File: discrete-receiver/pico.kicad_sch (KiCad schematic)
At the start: 48 parts, among them SW1 Reset, SW2 Select, SW3 Enter, U12 TPS7A20xxxDBV, U13 LM66100DCK, U14 LM66100DCK, U15 LM66100DCK, U6 RP2350A, U7 W25Q128JVS, U8 NCP1117-3.3_SOT223, Y1 ABM8-272-T3

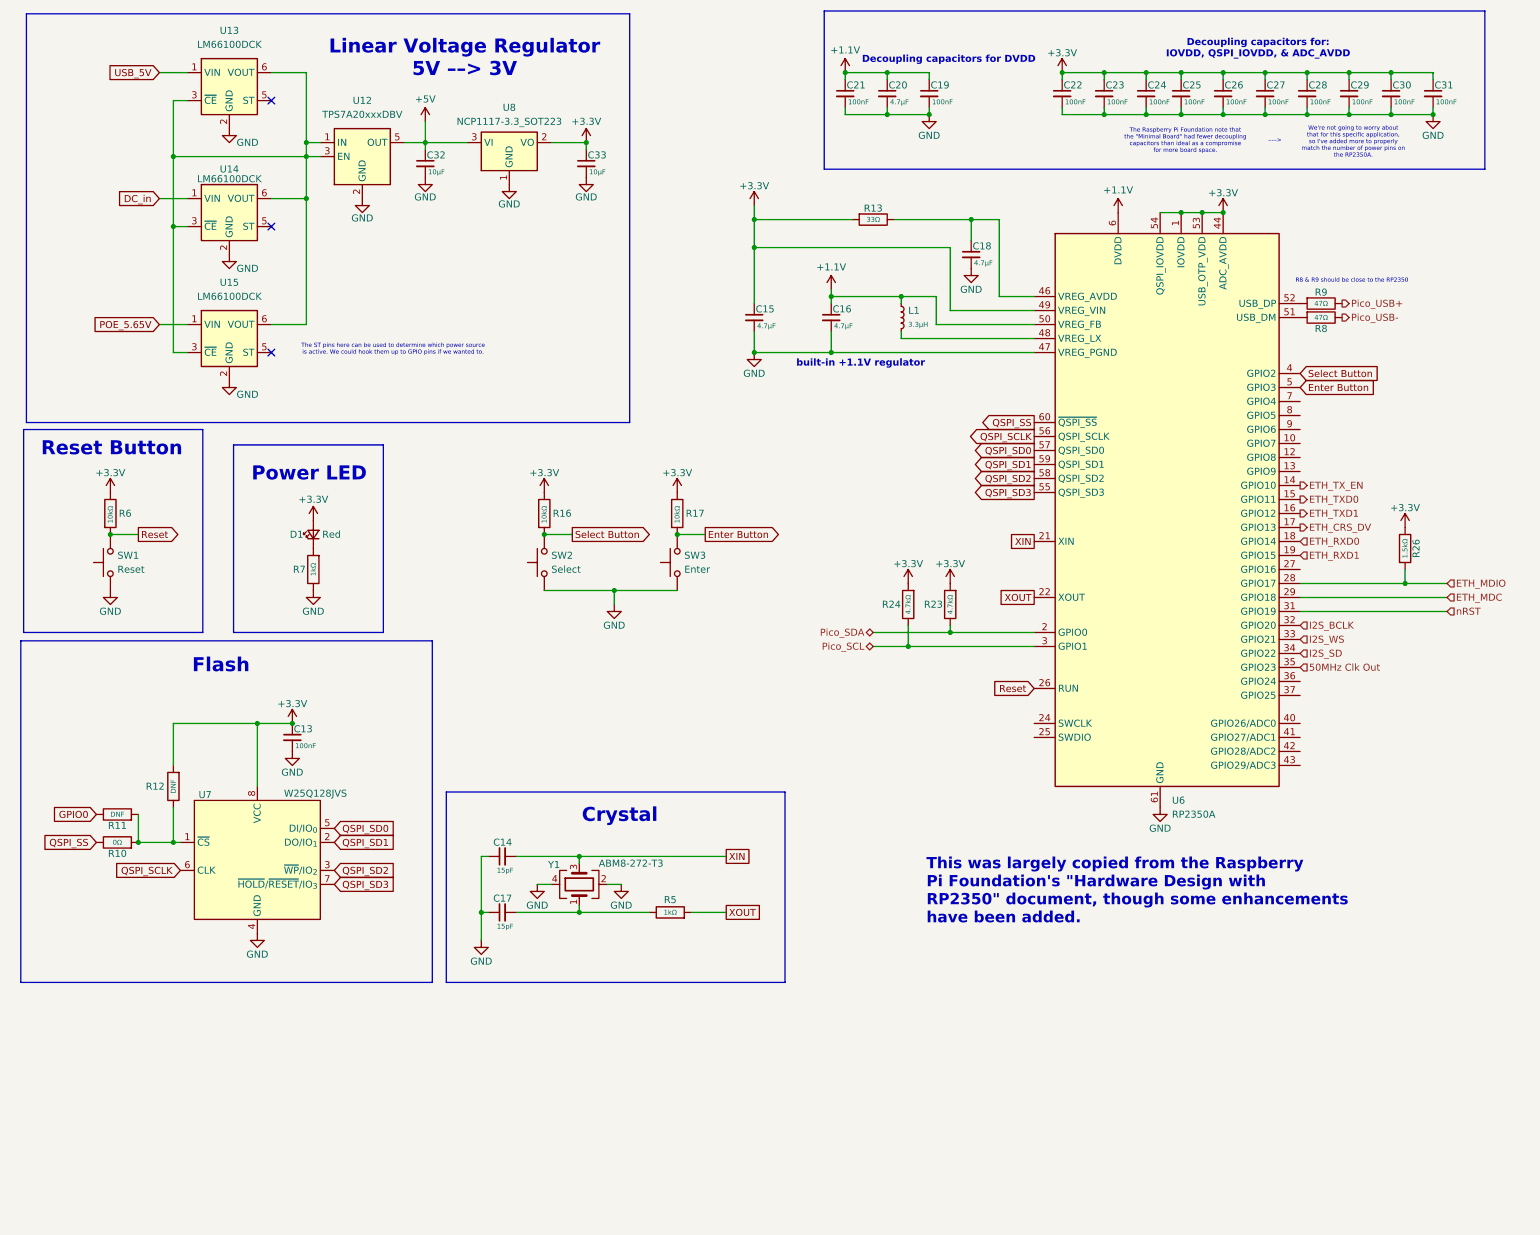
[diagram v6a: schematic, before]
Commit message: Updated components with JLCPCB details
Pico, receiver, and Ethernet interface sheets still contain basic components that have not been JLC'd yet. All sheets contain IC's that have not been JLC'd.
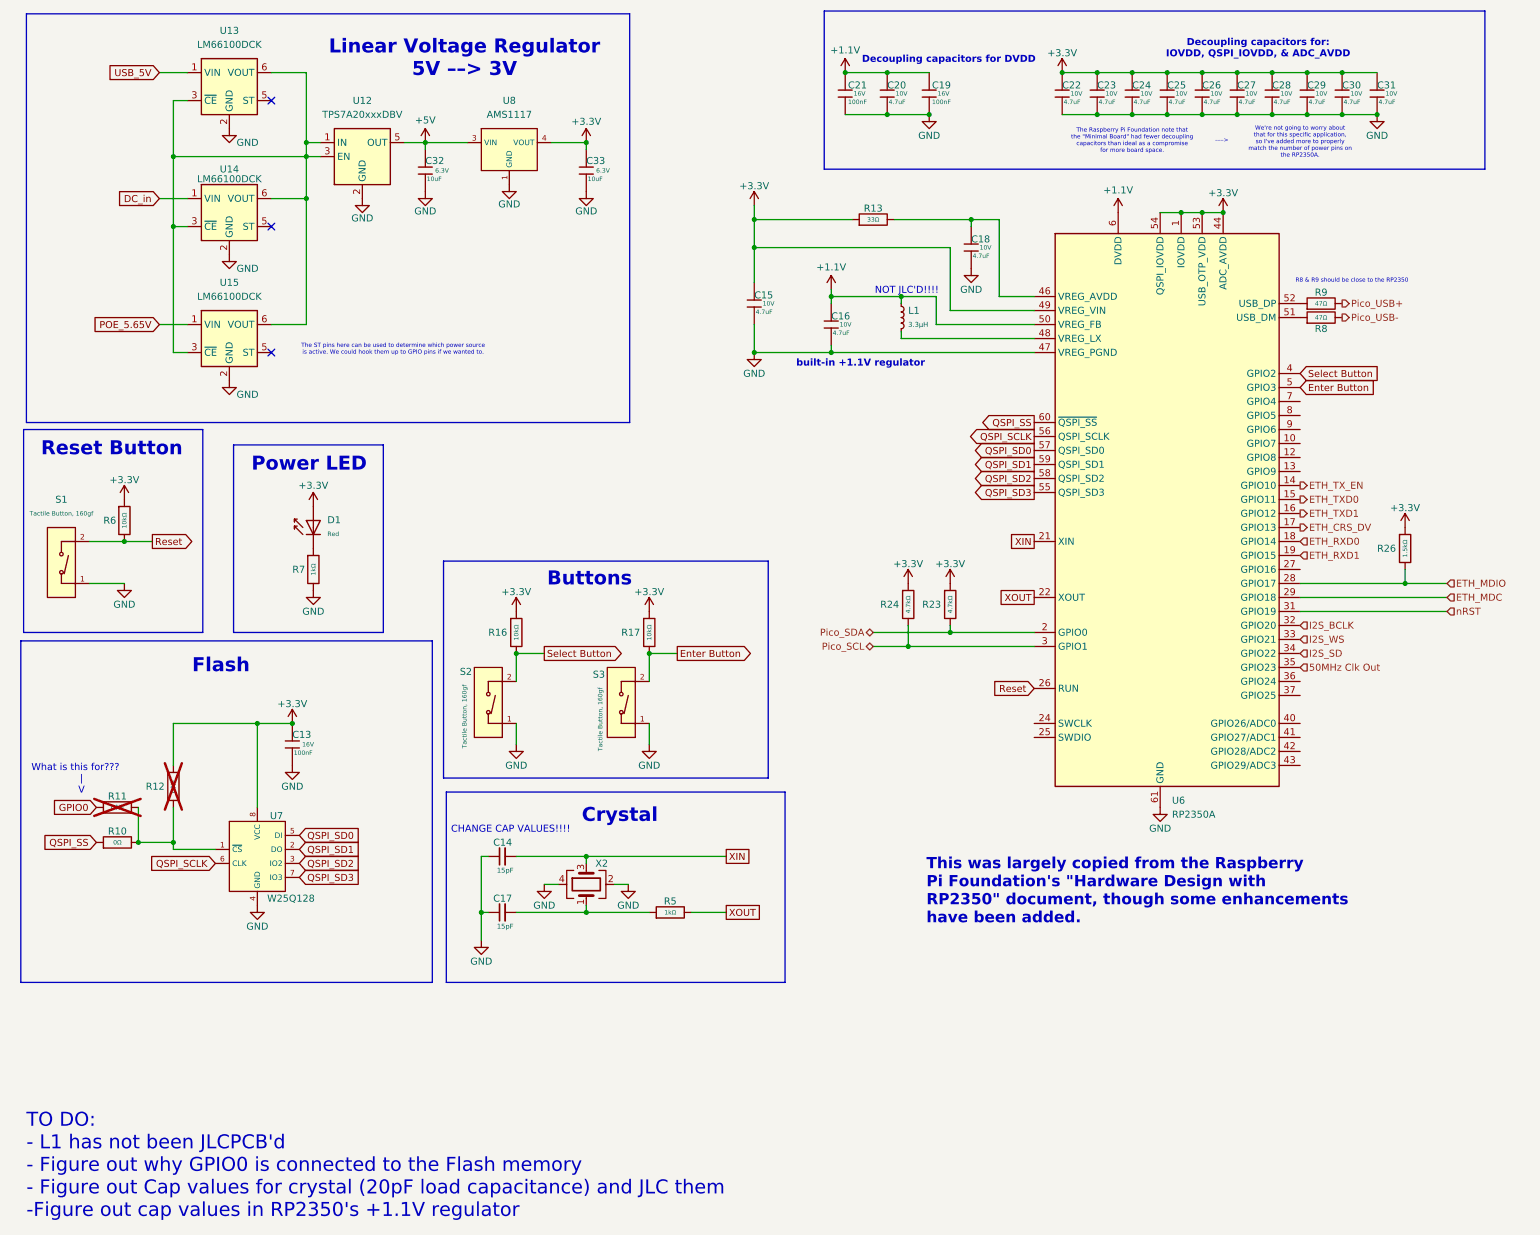
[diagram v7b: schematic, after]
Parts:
- removed C13, C19, C21, C22, C23, C24, C25, C26, C27, C28, C29, C30, C31: 100nF, symbol Device:C_Small
- removed C15, C16, C18, C20: 4.7µF, symbol Device:C_Small
- removed C32, C33: 10µF, symbol Device:C_Small
- removed D1: Red, symbol Device:LED_Small
- removed R10: 0Ω, symbol Device:R
- removed R13: 33Ω, symbol Device:R
- removed R16, R17, R6: 10kΩ, symbol Device:R
- removed R23, R24: 4.7kΩ, symbol Device:R
- removed R26: 1.5kΩ, symbol Device:R
- removed R5, R7: 1kΩ, symbol Device:R
- removed R8, R9: 47Ω, symbol Device:R
- removed SW1: Reset, symbol Switch:SW_Push
- removed SW2: Select, symbol Switch:SW_Push
- removed SW3: Enter, symbol Switch:SW_Push
- removed U7: W25Q128JVS, Package_SO:SOIC-8_5.3x5.3mm_P1.27mm, symbol Memory_Flash:W25Q128JVS
- removed U8: NCP1117-3.3_SOT223, Package_TO_SOT_SMD:SOT-223-3_TabPin2, symbol Regulator_Linear:NCP1117-3.3_SOT223
- removed Y1: ABM8-272-T3, sdr_project:ABM8-272-T3_ABR, symbol sdr_project:ABM8-272-T3
- added C13, C19, C21: 100nF, PCM_JLCPCB:C_0402, symbol PCM_JLCPCB-Capacitors:0402,100nF
- added C15, C16, C18, C20, C22, C23, C24, C25, C26, C27, C28, C29, C30, C31: 4.7uF, PCM_JLCPCB:C_0402, symbol PCM_JLCPCB-Capacitors:0402,4.7uF
- added C32, C33: 10uF, PCM_JLCPCB:C_0402, symbol PCM_JLCPCB-Capacitors:0402,10uF
- added D1: Red, PCM_JLCPCB:D_0603, symbol PCM_JLCPCB-Diodes:LED,0603,Red
- added R10: 0Ω, PCM_JLCPCB:R_0402, symbol PCM_JLCPCB-Resistors:0402,0Ω
- added R13: 33Ω, PCM_JLCPCB:R_0402, symbol PCM_JLCPCB-Resistors:0402,33Ω
- added R16, R17, R6: 10kΩ, PCM_JLCPCB:R_0402, symbol PCM_JLCPCB-Resistors:0402,10kΩ
- added R23, R24: 4.7kΩ, PCM_JLCPCB:R_0402, symbol PCM_JLCPCB-Resistors:0402,4.7kΩ
- added R26: 1.5kΩ, PCM_JLCPCB:R_0402, symbol PCM_JLCPCB-Resistors:0402,1.5kΩ
- added R5, R7: 1kΩ, PCM_JLCPCB:R_0402, symbol PCM_JLCPCB-Resistors:0402,1kΩ
- added R8, R9: 47Ω, PCM_JLCPCB:R_0402, symbol PCM_JLCPCB-Resistors:0402,47Ω
- added S1, S2, S3: Tactile Button, 160gf, PCM_JLCPCB:SW_TS-1088-AR02016, symbol PCM_JLCPCB-Connectors_Buttons:Tactile Button, 160gf, 12V, 50mA, 4.0mm
- added U7: W25Q128, PCM_JLCPCB:SOIC-8_L5.3-W5.3-P1.27-LS8.0-BL, symbol PCM_JLCPCB-Memory:16MByte, SPI
- added U8: AMS1117, PCM_JLCPCB:SOT-223-3_L6.5-W3.4-P2.30-LS7.0-BR, symbol PCM_JLCPCB-Power:LDO, 3.3V, 1A
- added X2: X322512MSB4SI, PCM_JLCPCB:CRYSTAL-SMD_4P-L3.2-W2.5-BL, symbol PCM_JLCPCB-Crystals:Crystal, 12MHz, 20pF
- R11, R12: now not fitted
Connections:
- net +1.1V: now also C16.1, C19.1, C20.1, C21.1
- net +3.3V: now also C13.1, C15.1, C22.1, C23.1, C24.1, C25.1, C26.1, C27.1, C28.1, C29.1, C30.1, C31.1, C33.1, D1.2, R13.1, R16.1, R17.1, R23.1, R24.1, R26.1, R6.1, U7.8 (VCC), U8.2 (VOUT), U8.4 (VOUT)
- net +5V: now also C32.1, U8.3 (VIN)
- net ETH_MDIO: now also R26.2
- net Enter Button: now also R17.2, S3.2 (B)
- net GND: now also C13.2, C15.2, C16.2, C18.2, C19.2, C20.2, C21.2, C22.2, C23.2, C24.2, C25.2, C26.2, C27.2, C28.2, C29.2, C30.2, C31.2, C32.2, C33.2, R7.2, S1.1 (A), S2.1 (A), S3.1 (A), U7.4 (GND), U8.1 (GND), X2.2, X2.4
- net Pico_SCL: now also R24.2
- net Pico_SDA: now also R23.2
- net Pico_USB+: now also R9.2
- net Pico_USB-: now also R8.2
- net QSPI_SCLK: now also U7.6 (CLK)
- net QSPI_SD0: now also U7.5 (DI)
- net QSPI_SD1: now also U7.2 (DO)
- net QSPI_SD2: now also U7.3 (IO2)
- net QSPI_SD3: now also U7.7 (IO3)
- net QSPI_SS: now also R10.1
- net Reset: now also R6.2, S1.2 (B)
- net Select Button: now also R16.2, S2.2 (B)
- net XIN: now also X2.3
- net XOUT: now also R5.2
- net at U6.51 (USB_DM): now also R8.1
- net at C17.2: now also R5.1, X2.1
- net at R11.2, R12.1: now also R10.2, U7.1 (~{CS})
- net at U6.46 (VREG_AVDD): now also C18.1, R13.2
- net at U6.52 (USB_DP): now also R9.1
- new net: D1.1, R7.1
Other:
- note added: "Buttons"
- note added: "CHANGE CAP VALUES!!!!"
- note added: "NOT JLC'D!!!!"
- note added: "TO DO: - L1 has not been JLCPCB'd - Figure out why GPIO0 is connected to the Flash memory - Figure out Cap values for crystal (20pF load capacitance) and JLC them -Figure out cap values in RP2350's +1.1V regulator"
- note added: "What is this for??? | V"

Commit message: Added more details and additions
Added power page and added a backup ADC.
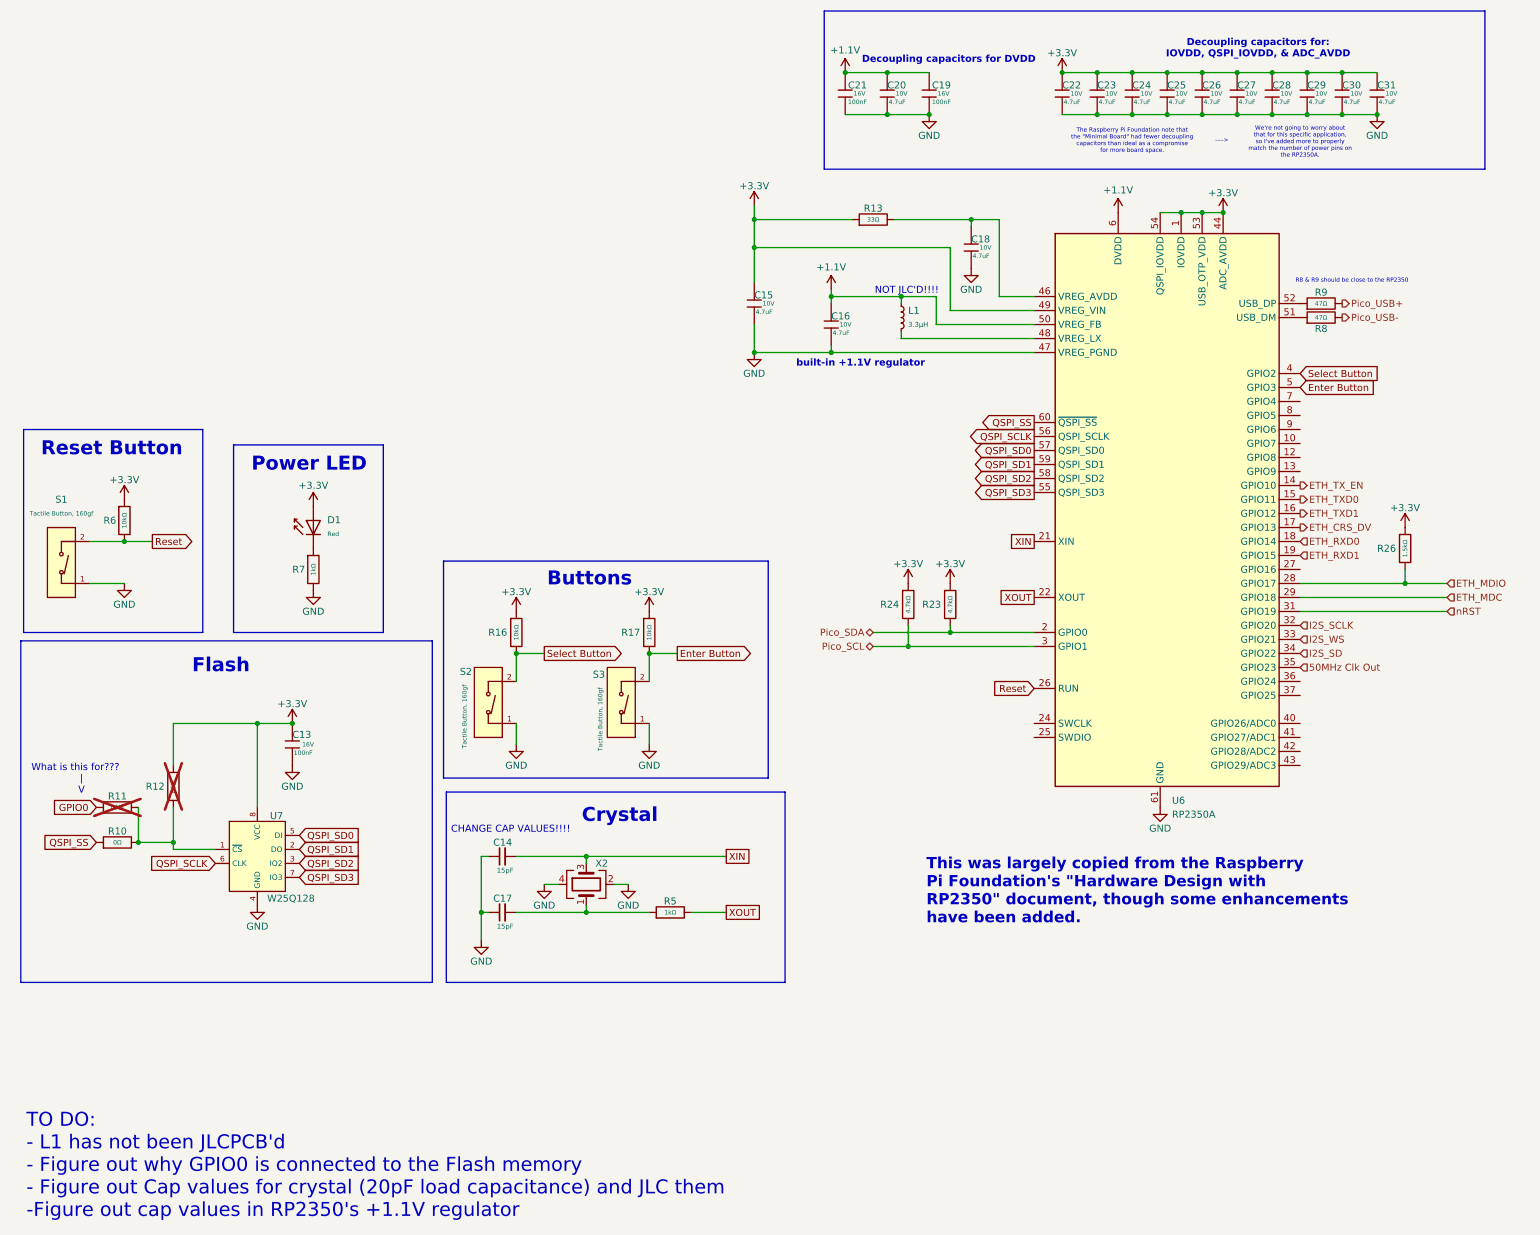
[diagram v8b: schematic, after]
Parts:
- removed C32, C33: 10uF, PCM_JLCPCB:C_0402, symbol PCM_JLCPCB-Capacitors:0402,10uF
- removed U12: TPS7A20xxxDBV, Package_TO_SOT_SMD:SOT-23-5, symbol Regulator_Linear:TPS7A20xxxDBV
- removed U13, U14, U15: LM66100DCK, Package_TO_SOT_SMD:SOT-363_SC-70-6, symbol Power_Management:LM66100DCK
- removed U8: AMS1117, PCM_JLCPCB:SOT-223-3_L6.5-W3.4-P2.30-LS7.0-BR, symbol PCM_JLCPCB-Power:LDO, 3.3V, 1A
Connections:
- net I2S_BCLK renamed I2S_SCLK
- no-connect marks 3 -> 0
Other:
- note removed: "Linear Voltage Regulator 5V ––> 3V"
- note removed: "The ST pins here can be used to determine which power source is active. We could hook them up to GPIO pins if we wanted to."
